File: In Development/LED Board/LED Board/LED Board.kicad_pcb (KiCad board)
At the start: 2 copper layers, 30 x 30 mm, 9 parts, among them J1 Screw_Terminal_01x03, U1 AL5802

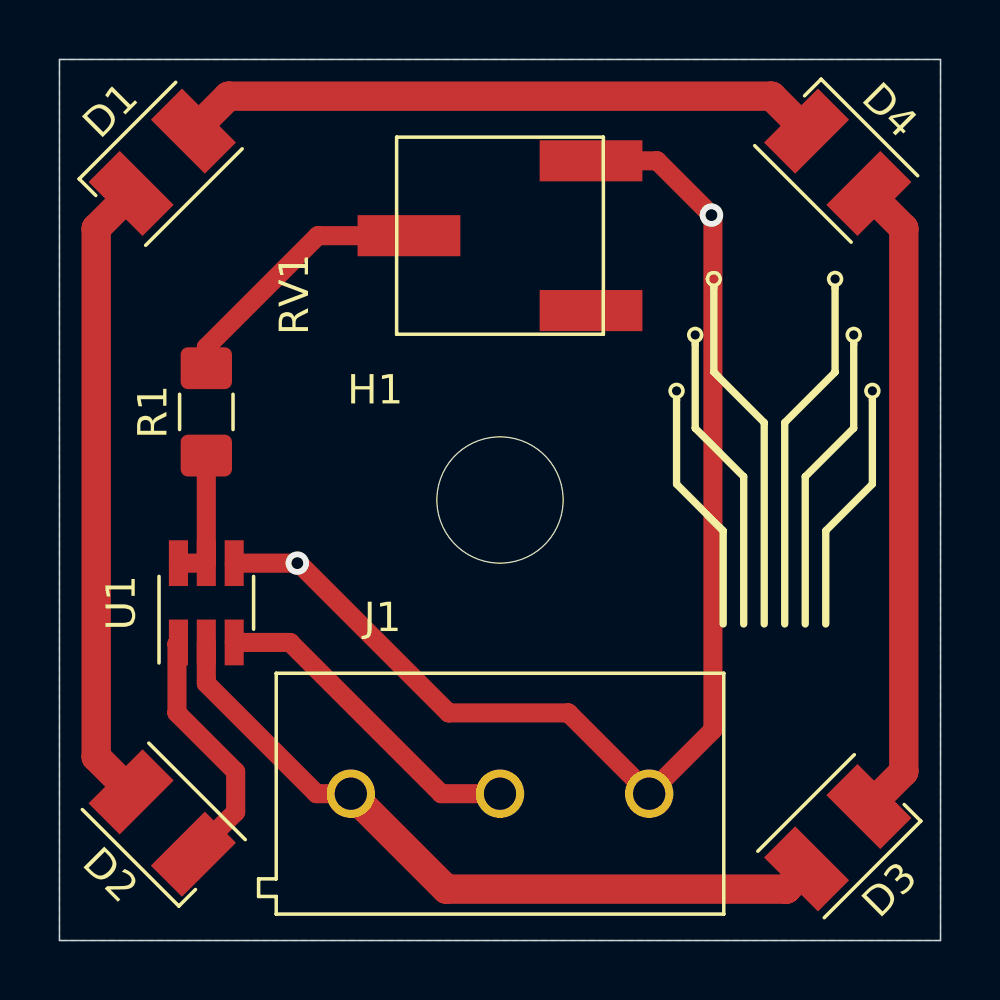
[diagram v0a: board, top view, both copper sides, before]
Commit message: better via placement, silkscreen
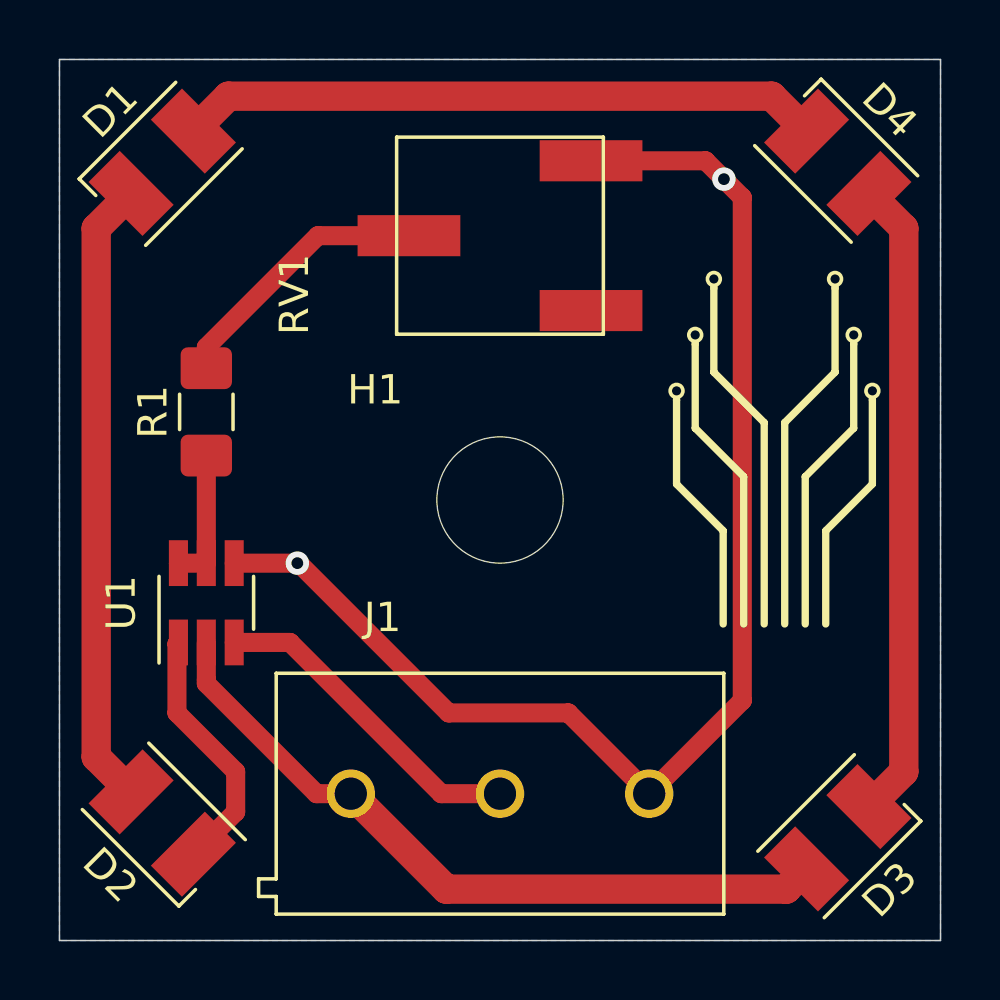
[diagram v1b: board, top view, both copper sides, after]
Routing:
- net GND: track 42.9 -> 44.7 mm
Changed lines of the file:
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@@
   (segment (start 127.56066 95.43934) (end 128.75 94.25) (width 1) (layer F.Cu) (net 4))
   (segment (start 128.75 94.25) (end 128.75 75.75) (width 1) (layer F.Cu) (net 4))
-  (segment (start 122.25 92.83) (end 122.25 75.35) (width 0.65) (layer F.Cu) (net 5))
-  (segment (start 122.25 75.35) (end 122.2 75.3) (width 0.65) (layer F.Cu) (net 5))
-  (segment (start 120.08 95) (end 122.25 92.83) (width 0.65) (layer F.Cu) (net 5))
   (segment (start 108.1 87.15) (end 105.95 87.15) (width 0.65) (layer F.Cu) (net 5))
   (via (at 108.1 87.15) (size 0.8) (drill 0.4) (layers F.Cu B.Cu) (net 5))
-  (via (at 122.2 75.3) (size 0.8) (drill 0.4) (layers F.Cu B.Cu) (net 5))
   (segment (start 108.15 87.15) (end 108.1 87.15) (width 0.65) (layer F.Cu) (net 5))
   (segment (start 113.25 92.25) (end 108.15 87.15) (width 0.65) (layer F.Cu) (net 5))
   (segment (start 120.08 95) (end 117.33 92.25) (width 0.65) (layer F.Cu) (net 5))
   (segment (start 117.33 92.25) (end 113.25 92.25) (width 0.65) (layer F.Cu) (net 5))
-  (segment (start 122.2 75.3) (end 120.35 73.45) (width 0.65) (layer F.Cu) (net 5))
-  (segment (start 120.35 73.45) (end 118.1 73.45) (width 0.65) (layer F.Cu) (net 5))
+  (segment (start 122 73.45) (end 118.1 73.45) (width 0.65) (layer F.Cu) (net 5))
+  (segment (start 123.25 74.7) (end 122.625 74.075) (width 0.65) (layer F.Cu) (net 5))
+  (segment (start 120.08 95) (end 123.25 91.83) (width 0.65) (layer F.Cu) (net 5))
+  (segment (start 123.25 91.83) (end 123.25 74.7) (width 0.65) (layer F.Cu) (net 5))
+  (segment (start 122.625 74.075) (end 122 73.45) (width 0.65) (layer F.Cu) (net 5))
+  (via (at 122.625 74.075) (size 0.8) (drill 0.4) (layers F.Cu B.Cu) (net 5))
   (segment (start 107.85 89.85) (end 105.95 89.85) (width 0.65) (layer F.Cu) (net 6))
   (segment (start 113 95) (end 107.85 89.85) (width 0.65) (layer F.Cu) (net 6))

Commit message: thermals improved, a lot.
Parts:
- moved D2 0.50 mm to (103.5, 96.5)
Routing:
- net Net-(R1-Pad2): track 8.94 -> 13.9 mm, vias 0 -> 3
- net Net-(R1-Pad1): track 4.61 -> 8.12 mm, vias 0 -> 4
- net GND: track 44.7 -> 47.1 mm, vias 2 -> 4
- net /EN: track 11.2 -> 13.3 mm, vias 0 -> 2
- net Net-(D2-Pad1): track 8.66 -> 10.8 mm, vias 0 -> 8
- net Net-(D3-Pad1): vias 0 -> 3
- net Net-(D1-Pad2): vias 0 -> 3
- net Net-(D1-Pad1): vias 0 -> 3
- added copper zone on B.Cu, net /EN
- added copper zone on F.Cu, net /EN
- added copper zone on F.Cu, net GND
- added copper zone on B.Cu, net Net-(D1-Pad1)
- added copper zone on B.Cu, net Net-(D1-Pad2)
- added copper zone on B.Cu, net Net-(D2-Pad1)
- added copper zone on F.Cu, net Net-(D2-Pad1)
- added copper zone on B.Cu, net Net-(D3-Pad1)
- added copper zone on B.Cu, net Net-(R1-Pad1)
- added copper zone on F.Cu, net Net-(R1-Pad1)
- added copper zone on B.Cu, net Net-(R1-Pad2)
- added copper zone on F.Cu, net Net-(R1-Pad2)
- added copper zone on B.Cu, net VCC

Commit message: Mild edits.
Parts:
- moved R1 0.90 mm to (105.0, 81.1)
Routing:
- net GND: track 47.1 -> 50.1 mm, vias 4 -> 5
- net Net-(R1-Pad1): track 8.12 -> 10.5 mm
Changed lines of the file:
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@@
     (thickness 1.6)
     (drawings 467)
-    (tracks 84)
+    (tracks 87)
     (zones 0)
     (modules 9)
@@
     (34 B.Paste user)
     (35 F.Paste user)
-    (36 B.SilkS user hide)
-    (37 F.SilkS user hide)
+    (36 B.SilkS user)
+    (37 F.SilkS user)
     (38 B.Mask user)
     (39 F.Mask user)
@@
   )
   (module Resistor_SMD:R_1206_3216Metric_Pad1.42x1.75mm_HandSolder (layer F.Cu)
-    (at 105 82 90)
+    (at 105 81.1 90)
     (descr "Resistor SMD 1206 (3216 Metric), square (rectangular) end terminal, IPC_7351 nominal with elongated pad for handsoldering. (Body size source: http://www.tortai-tech.com/upload/download/2011102023233369053.pdf), generated with kicad-footprint-generator")
     (tags "resistor handsolder")
@@
   (gr_line (start 130 100) (end 130 70) (layer Edge.Cuts) (width 0.05))
   (gr_line (start 100 100) (end 130 100) (layer Edge.Cuts) (width 0.05))
-  (via (at 101.25 80) (size 1) (drill 0.5) (layers F.Cu B.Cu) (net 2))
-  (via (at 101.25 90) (size 1) (drill 0.5) (layers F.Cu B.Cu) (net 2))
-  (via (at 110 71.25) (size 1) (drill 0.5) (layers F.Cu B.Cu) (net 10))
+  (via (at 107.2 87.1) (size 0.8) (drill 0.4) (layers F.Cu B.Cu) (net 5))
   (segment (start 124.75 98.25) (end 125.43934 97.56066) (width 1) (layer F.Cu) (net 1))
   (segment (start 109.92 95) (end 113.17 98.25) (width 1) (layer F.Cu) (net 1))
@@
   (segment (start 109.92 95) (end 109.078 94.158) (width 0.65) (layer F.Cu) (net 1))
   (segment (start 109.078 94.158) (end 107.911274 94.158) (width 0.65) (layer F.Cu) (net 1))
+  (via (at 101.25 80) (size 1) (drill 0.5) (layers F.Cu B.Cu) (net 2))
+  (via (at 101.25 90) (size 1) (drill 0.5) (layers F.Cu B.Cu) (net 2))
   (segment (start 101.25 93.75) (end 102.43934 94.93934) (width 1) (layer F.Cu) (net 2))
   (segment (start 102.43934 74.56066) (end 101.25 75.75) (width 1) (layer F.Cu) (net 2))
@@
   (via (at 128.75 90) (size 1) (drill 0.5) (layers F.Cu B.Cu) (net 4))
   (segment (start 108.1 87.15) (end 105.95 87.15) (width 0.65) (layer F.Cu) (net 5))
-  (via (at 108.1 87.15) (size 0.8) (drill 0.4) (layers F.Cu B.Cu) (net 5))
   (segment (start 108.15 87.15) (end 108.1 87.15) (width 0.65) (layer F.Cu) (net 5))
   (segment (start 113.25 92.25) (end 108.15 87.15) (width 0.65) (layer F.Cu) (net 5))
   (segment (start 120.08 95) (end 117.33 92.25) (width 0.65) (layer F.Cu) (net 5))
   (segment (start 117.33 92.25) (end 113.25 92.25) (width 0.65) (layer F.Cu) (net 5))
-  (via (at 108.7 83) (size 0.8) (drill 0.4) (layers F.Cu B.Cu) (net 5))
-  (via (at 108.7 84.5) (size 0.8) (drill 0.4) (layers F.Cu B.Cu) (net 5))
-  (via (at 108.7 86) (size 0.8) (drill 0.4) (layers F.Cu B.Cu) (net 5))
-  (segment (start 108.7 83) (end 108.7 84) (width 0.5) (layer F.Cu) (net 5))
-  (segment (start 108.7 84) (end 108.7 85) (width 0.5) (layer F.Cu) (net 5))
-  (segment (start 108.7 85) (end 108.7 86) (width 0.5) (layer F.Cu) (net 5))
+  (via (at 108.7 82.6) (size 0.8) (drill 0.4) (layers F.Cu B.Cu) (net 5))
+  (via (at 108.7 84.1) (size 0.8) (drill 0.4) (layers F.Cu B.Cu) (net 5))
+  (via (at 108.7 85.6) (size 0.8) (drill 0.4) (layers F.Cu B.Cu) (net 5))
+  (segment (start 108.7 82.5) (end 108.7 83.5) (width 0.5) (layer F.Cu) (net 5))
+  (segment (start 108.7 83.5) (end 108.7 84.5) (width 0.5) (layer F.Cu) (net 5))
+  (segment (start 108.7 84.5) (end 108.7 85.5) (width 0.5) (layer F.Cu) (net 5))
   (segment (start 123.25 75.65) (end 121.05 73.45) (width 1) (layer F.Cu) (net 5))
   (segment (start 120.08 95) (end 123.25 91.83) (width 1) (layer F.Cu) (net 5))
   (segment (start 121.05 73.45) (end 118.1 73.45) (width 1) (layer F.Cu) (net 5))
   (segment (start 123.25 91.83) (end 123.25 75.65) (width 1) (layer F.Cu) (net 5))
+  (via (at 108.7 87.1) (size 0.8) (drill 0.4) (layers F.Cu B.Cu) (net 5))
+  (segment (start 108.7 85.5) (end 108.7 87) (width 0.5) (layer F.Cu) (net 5))
+  (segment (start 107.2 87.1) (end 108.7 87.1) (width 0.5) (layer F.Cu) (net 5))
   (segment (start 107.85 89.85) (end 105.95 89.85) (width 0.65) (layer F.Cu) (net 6))
   (segment (start 113 95) (end 107.85 89.85) (width 0.65) (layer F.Cu) (net 6))
   (segment (start 115 95) (end 113 95) (width 0.65) (layer F.Cu) (net 6))
-  (via (at 108.89 92.38) (size 0.8) (drill 0.4) (layers F.Cu B.Cu) (net 6))
-  (via (at 107.366 90.856) (size 0.8) (drill 0.4) (layers F.Cu B.Cu) (net 6))
-  (segment (start 107.366 90.856) (end 108.89 92.38) (width 0.5) (layer F.Cu) (net 6))
-  (segment (start 105 80.5125) (end 105 79.8) (width 0.65) (layer F.Cu) (net 7))
-  (segment (start 108.8 76) (end 111.65 76) (width 0.65) (layer F.Cu) (net 7))
-  (segment (start 105 79.8) (end 108.8 76) (width 0.65) (layer F.Cu) (net 7))
+  (via (at 109.2 92.7) (size 0.8) (drill 0.4) (layers F.Cu B.Cu) (net 6))
+  (segment (start 108 91.5) (end 109.2 92.7) (width 0.5) (layer F.Cu) (net 6))
+  (via (at 108 91.5) (size 0.8) (drill 0.4) (layers F.Cu B.Cu) (net 6))
   (via (at 108.25 73) (size 0.8) (drill 0.4) (layers F.Cu B.Cu) (net 7))
   (via (at 110.75 73) (size 0.8) (drill 0.4) (layers F.Cu B.Cu) (net 7))
@@
   (segment (start 108.25 73) (end 110.75 73) (width 0.5) (layer F.Cu) (net 7))
   (segment (start 110.75 73) (end 113.25 73) (width 0.5) (layer F.Cu) (net 7))
-  (segment (start 105 87.15) (end 105 83.4875) (width 0.65) (layer F.Cu) (net 8))
+  (segment (start 105 78.9) (end 105 79.6125) (width 0.65) (layer F.Cu) (net 7))
+  (segment (start 111.9 76) (end 107.9 76) (width 0.65) (layer F.Cu) (net 7))
+  (segment (start 107.9 76) (end 105 78.9) (width 0.65) (layer F.Cu) (net 7))
   (segment (start 104.05 87.15) (end 105 87.15) (width 0.65) (layer F.Cu) (net 8))
-  (via (at 106.7 83.5) (size 0.8) (drill 0.4) (layers F.Cu B.Cu) (net 8))
-  (via (at 103.3 83.49) (size 0.8) (drill 0.4) (layers F.Cu B.Cu) (net 8))
-  (segment (start 103.3 83.49) (end 103.3 85.2) (width 0.5) (layer F.Cu) (net 8))
-  (via (at 103.3 85.2) (size 0.8) (drill 0.4) (layers F.Cu B.Cu) (net 8))
-  (segment (start 106.7 83.5) (end 106.7 85.3) (width 0.5) (layer F.Cu) (net 8))
-  (via (at 106.7 85.3) (size 0.8) (drill 0.4) (layers F.Cu B.Cu) (net 8))
+  (via (at 106.7 82.6) (size 0.8) (drill 0.4) (layers F.Cu B.Cu) (net 8))
+  (via (at 103.3 82.6) (size 0.8) (drill 0.4) (layers F.Cu B.Cu) (net 8))
+  (via (at 103.3 85.1) (size 0.8) (drill 0.4) (layers F.Cu B.Cu) (net 8))
+  (via (at 106.7 85.1) (size 0.8) (drill 0.4) (layers F.Cu B.Cu) (net 8))
+  (segment (start 103.3 82.6) (end 103.3 85.1) (width 0.5) (layer F.Cu) (net 8))
+  (segment (start 106.7 82.6) (end 106.7 85.1) (width 0.5) (layer F.Cu) (net 8))
+  (segment (start 105 87.15) (end 105 82.5875) (width 0.65) (layer F.Cu) (net 8))
+  (via (at 110 71.25) (size 1) (drill 0.5) (layers F.Cu B.Cu) (net 10))
   (segment (start 105.75 71.25) (end 104.56066 72.43934) (width 1) (layer F.Cu) (net 10))
   (segment (start 125.43934 72.43934) (end 124.25 71.25) (width 1) (layer F.Cu) (net 10))
@@
     (polygon
       (pts
-        (xy 107.3 85.8) (xy 105 85.8) (xy 105 87.9096) (xy 102.3 87.9) (xy 102.3 82.8)
-        (xy 107.3 82.8)
+        (xy 107.3 85.8) (xy 105 85.8) (xy 105 87.9096) (xy 102.3 87.9) (xy 102.3 81.9)
+        (xy 107.3 81.9)
       )
     )
@@
     (polygon
       (pts
-        (xy 113.8 72.5) (xy 113.7 79.4) (xy 109 79.4) (xy 109 81.1) (xy 104.15 81.1)
-        (xy 104.1 76.8) (xy 107.7 73.25) (xy 107.7 72.5)
+        (xy 113.8 72.5) (xy 113.7 79.4) (xy 109 79.4) (xy 109 80.3) (xy 102.5 80.3)
+        (xy 102.5 78.6) (xy 107.7 73.25) (xy 107.7 72.5)
       )
     )
@@
     (polygon
       (pts
-        (xy 107.3 85.8) (xy 105 85.8) (xy 105 87.9096) (xy 102.4 87.9) (xy 102.4 82)
-        (xy 107.3 82)
+        (xy 107.3 85.8) (xy 105 85.8) (xy 105 87.9096) (xy 102.4 87.9) (xy 102.4 81.5)
+        (xy 107.3 81.5)
       )
     )
@@
     (polygon
       (pts
-        (xy 117.1 79.95) (xy 108.9 79.9) (xy 108.9 81.2) (xy 102.4 81.2) (xy 102.4 78.3)
+        (xy 117.1 79.95) (xy 108.9 79.9) (xy 108.9 80.7) (xy 102.4 80.7) (xy 102.4 78.3)
         (xy 107 73.5) (xy 107 72.6) (xy 117.1 72.6)
       )
